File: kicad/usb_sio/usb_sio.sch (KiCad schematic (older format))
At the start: 24 parts, among them CON1 USB, P1 Z80_BUS_PINS, P2 IO_BUS_PINS, P3 CONN_02X05, U1 MCP2200, U2 68B50, U3 74HCT04, U4 1.8432MHz, Y1 12MHz

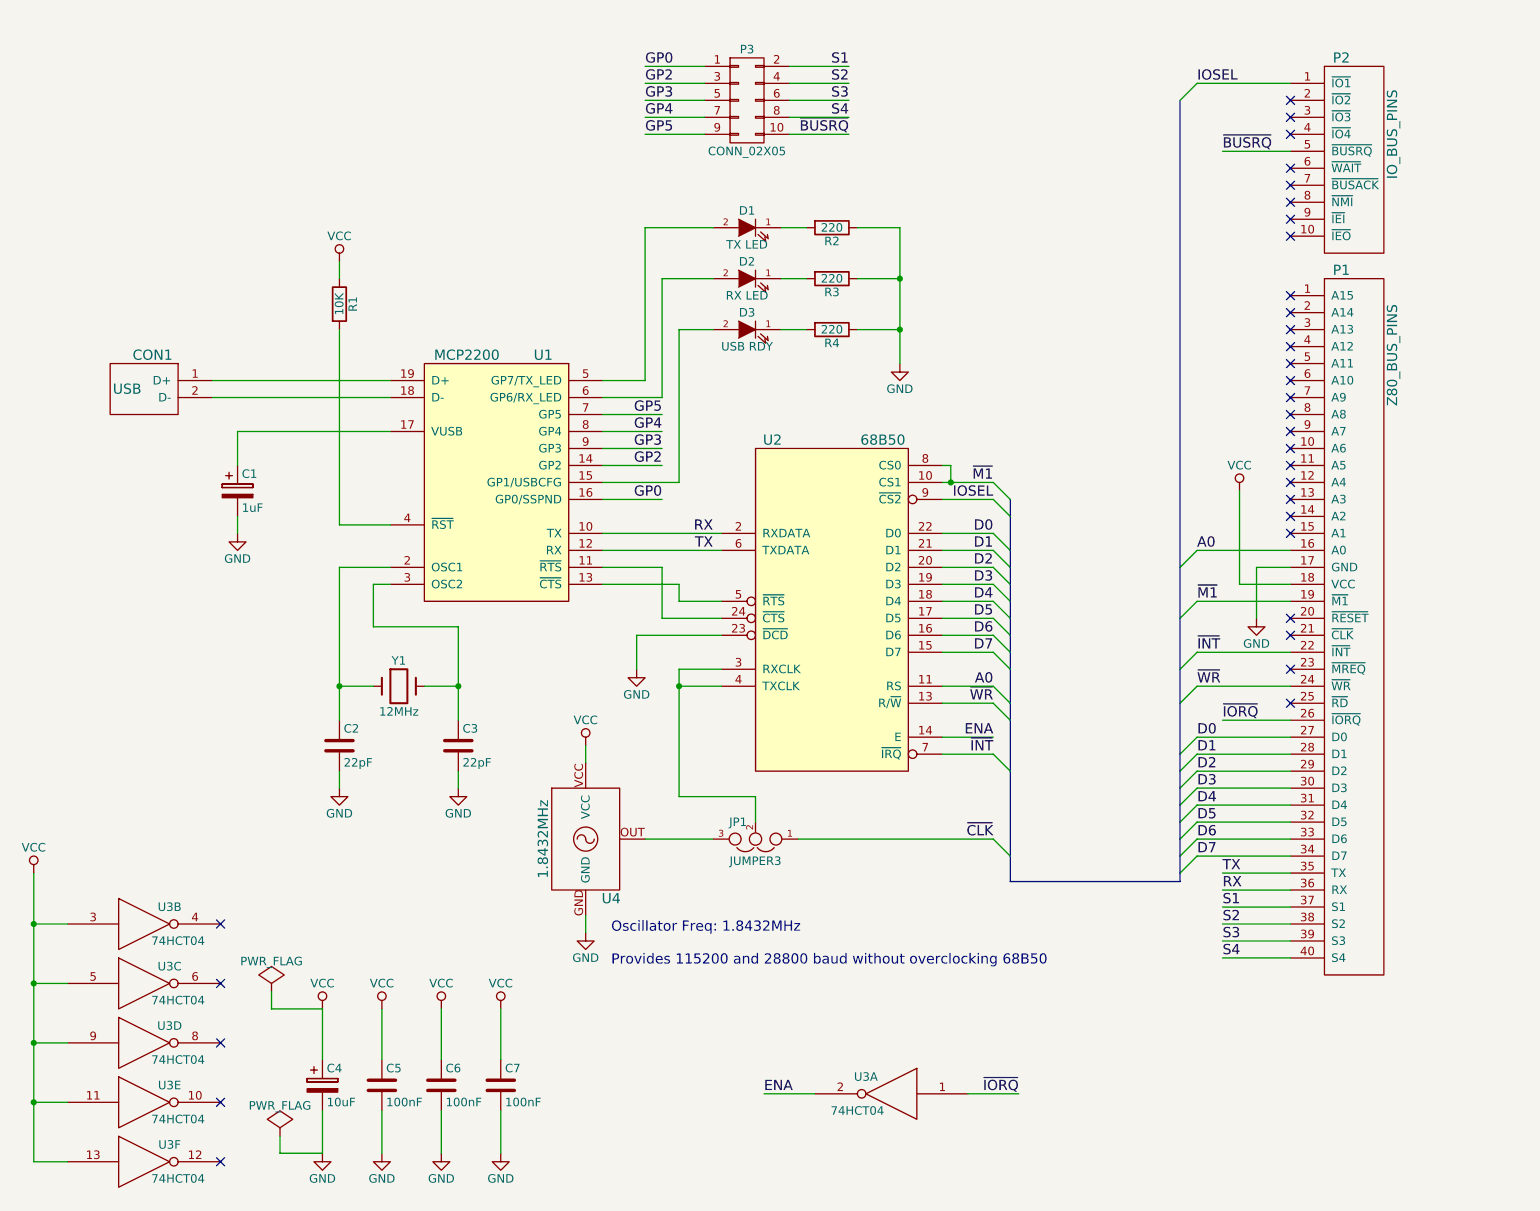
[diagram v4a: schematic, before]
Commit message: Fixed missing CLK like on SIO board
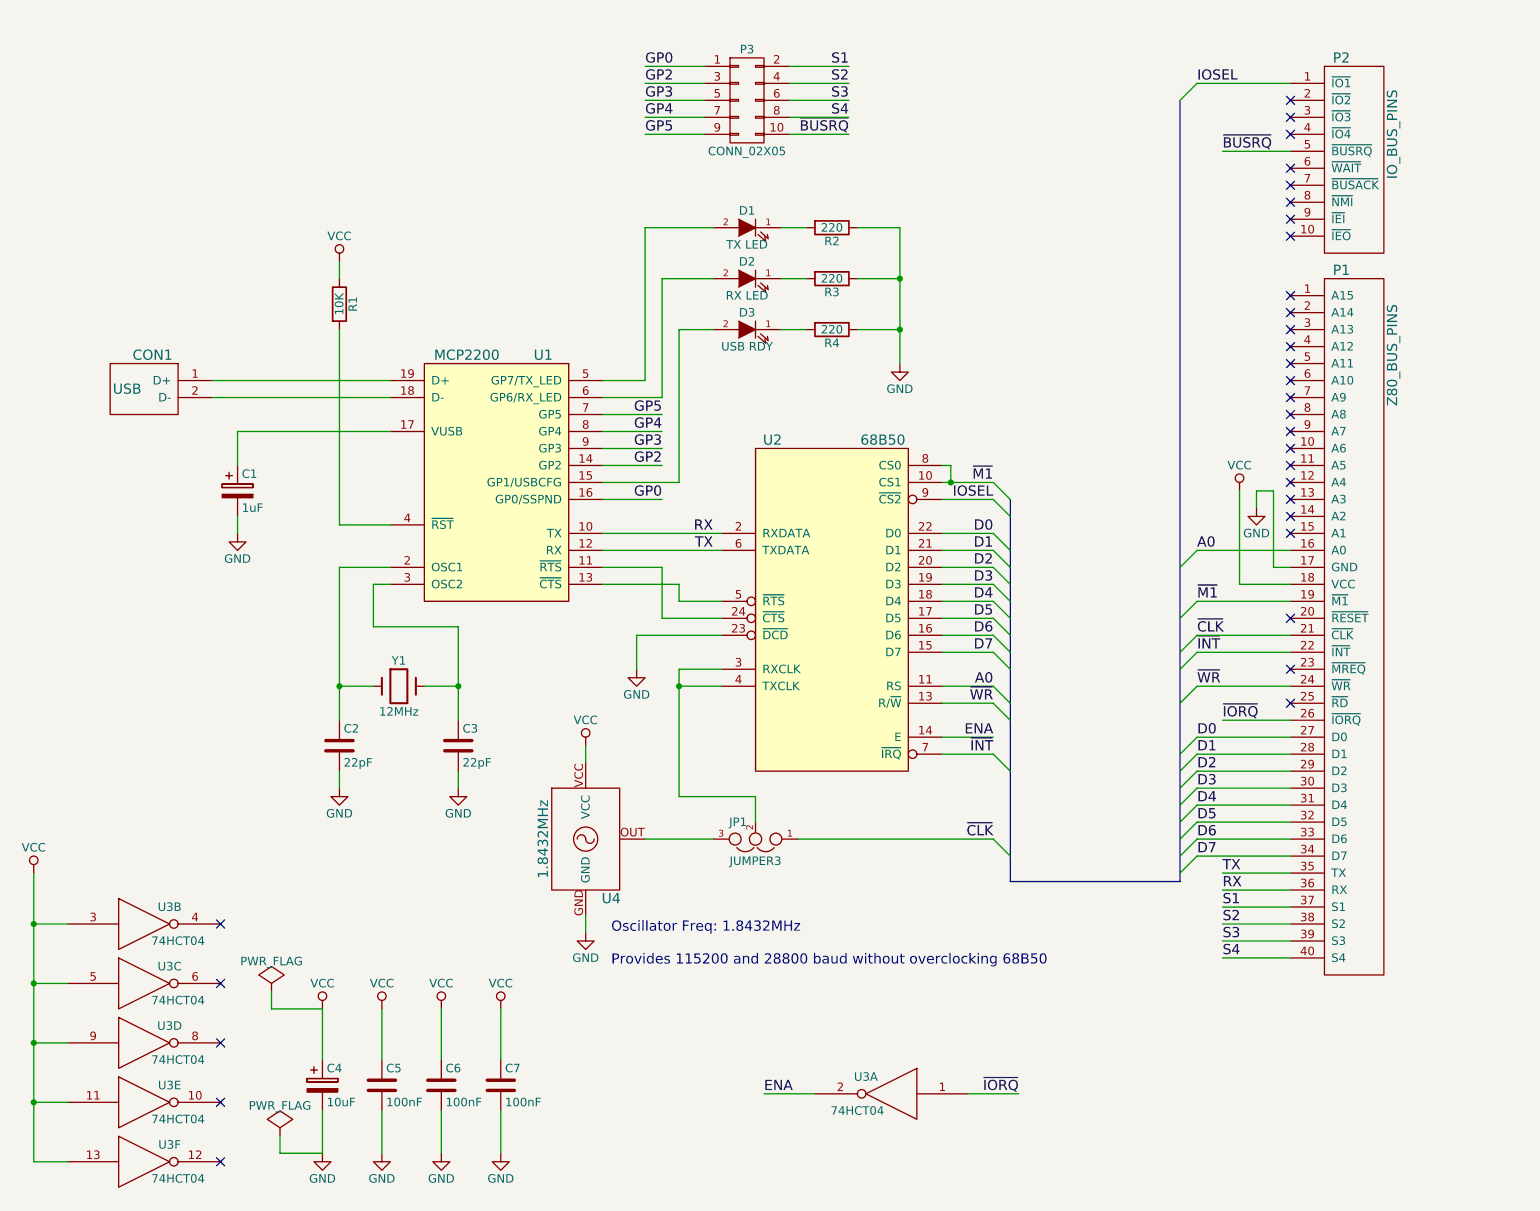
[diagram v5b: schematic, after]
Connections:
- net ~CLK: now also P1.21 (~CLK)
- no-connect marks 32 -> 31
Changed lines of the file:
@@
 NoConn ~ 8200 3700
 NoConn ~ 8200 4200
-NoConn ~ 8200 4300
 NoConn ~ 8200 4500
 NoConn ~ 8200 4700
@@
 L GND #PWR010
 U 1 1 57D54DB5
-P 8000 4200
-F 0 "#PWR010" H 8000 3950 50  0001 C CNN
-F 1 "GND" H 8000 4050 50  0000 C CNN
-F 2 "" H 8000 4200 50  0000 C CNN
-F 3 "" H 8000 4200 50  0000 C CNN
-	1    8000 4200
+P 8000 3550
+F 0 "#PWR010" H 8000 3300 50  0001 C CNN
+F 1 "GND" H 8000 3400 50  0000 C CNN
+F 2 "" H 8000 3550 50  0000 C CNN
+F 3 "" H 8000 3550 50  0000 C CNN
+	1    8000 3550
 	1    0    0    -1
 $EndComp
@@
 	2900 3900 2600 3900
 Wire Wire Line
-	2600 3900 2600 4600
-Wire Wire Line
-	2600 4600 2600 4800
+	2600 3900 2600 4800
 Wire Wire Line
 	2600 4600 2800 4600
@@
 	3100 4600 3300 4600
 Wire Wire Line
-	3300 4250 3300 4600
-Wire Wire Line
-	3300 4600 3300 4800
+	3300 4250 3300 4800
 Wire Wire Line
 	3300 4250 2800 4250
@@
 	4400 5500 4800 5500
 Wire Wire Line
-	4600 4500 4600 4600
-Wire Wire Line
-	4600 4600 4600 5250
+	4600 4500 4600 5250
 Wire Wire Line
 	4600 4500 4850 4500
@@
 	6150 4400 6450 4400
 Wire Bus Line
-	6550 3500 6550 3600
-Wire Bus Line
-	6550 3600 6550 3800
-Wire Bus Line
-	6550 3800 6550 3900
-Wire Bus Line
-	6550 3900 6550 4000
-Wire Bus Line
-	6550 4000 6550 4100
-Wire Bus Line
-	6550 4100 6550 4200
-Wire Bus Line
-	6550 4200 6550 4300
-Wire Bus Line
-	6550 4300 6550 4400
-Wire Bus Line
-	6550 4400 6550 4500
-Wire Bus Line
-	6550 4500 6550 4700
-Wire Bus Line
-	6550 4700 6550 4800
-Wire Bus Line
-	6550 4800 6550 5100
-Wire Bus Line
-	6550 5100 6550 5600
-Wire Bus Line
-	6550 5600 6550 5750
+	6550 3500 6550 5750
 Wire Bus Line
 	6550 5750 7550 5750
@@
 	6150 5000 6450 5000
 Wire Wire Line
-	6150 3400 6200 3400
-Wire Wire Line
-	6200 3400 6450 3400
+	6150 3400 6450 3400
 Wire Wire Line
 	6150 3500 6450 3500
@@
 	5300 5500 6450 5500
 Wire Bus Line
-	7550 5750 7550 5700
-Wire Bus Line
-	7550 5700 7550 5600
-Wire Bus Line
-	7550 5600 7550 5500
-Wire Bus Line
-	7550 5500 7550 5400
-Wire Bus Line
-	7550 5400 7550 5300
-Wire Bus Line
-	7550 5300 7550 5200
-Wire Bus Line
-	7550 5200 7550 5100
-Wire Bus Line
-	7550 5100 7550 5000
-Wire Bus Line
-	7550 5000 7550 4700
-Wire Bus Line
-	7550 4700 7550 4500
-Wire Bus Line
-	7550 4500 7550 4200
-Wire Bus Line
-	7550 4200 7550 3900
-Wire Bus Line
-	7550 3900 7550 1150
+	7550 5750 7550 1150
 Wire Wire Line
 	8200 1050 7650 1050
@@
 	5650 1900 5900 1900
 Wire Wire Line
-	5900 1900 5900 2200
-Wire Wire Line
-	5900 2200 5900 2500
-Wire Wire Line
-	5900 2500 5900 2700
+	5900 1900 5900 2700
 Wire Wire Line
 	5650 2500 5900 2500
@@
 	7800 1450 8200 1450
 Wire Wire Line
-	8200 3900 8000 3900
+	8100 3900 8200 3900
 Wire Wire Line
 	7900 4000 8200 4000
@@
 	7900 4000 7900 3450
 Wire Wire Line
-	8000 3900 8000 4200
-Wire Wire Line
 	6300 7000 6600 7000
 Wire Wire Line
 	8200 4800 7800 4800
 Wire Wire Line
-	800  5700 800  6000
-Wire Wire Line
-	800  6000 800  6350
-Wire Wire Line
-	800  6350 800  6700
-Wire Wire Line
-	800  6700 800  7050
-Wire Wire Line
-	800  7050 800  7400
+	800  5700 800  7400
 Wire Wire Line
 	800  7400 1000 7400
@@
 $EndComp
 Wire Wire Line
-	2500 6500 2500 6500
+	2200 6500 2500 6500
 Wire Wire Line
 	2500 6500 2500 6800
@@
 Wire Wire Line
 	2200 6400 2200 6500
-Wire Wire Line
-	2200 6500 2500 6500
-$Comp
-L PWR_FLAG #FLG?
+$Comp
+L PWR_FLAG #FLG021
 U 1 1 57D57677
 P 2250 7250
-F 0 "#FLG?" H 2250 7345 50  0001 C CNN
+F 0 "#FLG021" H 2250 7345 50  0001 C CNN
 F 1 "PWR_FLAG" H 2250 7430 50  0000 C CNN
 F 2 "" H 2250 7250 50  0000 C CNN
@@
 Wire Wire Line
 	2250 7350 2500 7350
+Wire Wire Line
+	8000 3550 8000 3450
+Wire Wire Line
+	8000 3450 8100 3450
+Wire Wire Line
+	8100 3450 8100 3900
+Entry Wire Line
+	7550 4400 7650 4300
+Wire Wire Line
+	7650 4300 8200 4300
+Text Label 7650 4300 0    60   ~ 0
+~CLK
 $EndSCHEMATC

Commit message: WIp on the SIO PCB
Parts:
- C1: footprint (none) -> Capacitors_ThroughHole:C_Radial_D5_L6_P2.5
- C2, C3: footprint (none) -> Capacitors_ThroughHole:C_Disc_D7.5_P5
- C4: footprint (none) -> Capacitors_ThroughHole:C_Radial_D6.3_L11.2_P2.5
- C5, C6, C7: footprint (none) -> Capacitors_ThroughHole:C_Disc_D3_P2.5
- CON1: footprint (none) -> Pin_Headers:Pin_Header_Angled_1x02
- D1, D2, D3: footprint (none) -> LEDs:LED-5MM
- JP1: footprint (none) -> Pin_Headers:Pin_Header_Straight_1x03
- P1: footprint (none) -> Pin_Headers:Pin_Header_Angled_1x40
- P2: footprint (none) -> Pin_Headers:Pin_Header_Angled_1x10
- P3: footprint (none) -> Pin_Headers:Pin_Header_Straight_2x05
- R1, R2, R3, R4: footprint (none) -> Resistors_ThroughHole:Resistor_Horizontal_RM10mm
- U1: footprint (none) -> Housings_DIP:DIP-20_W7.62mm_LongPads
- U2: footprint (none) -> Housings_DIP:DIP-24_W10.16mm_LongPads
- U3: footprint (none) -> Housings_DIP:DIP-14_W7.62mm_LongPads
- U4: footprint (none) -> Oscillators:OSC_DIP8
- Y1: footprint (none) -> Crystals:Crystal_HC49-U_Vertical
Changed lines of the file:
@@
 F 0 "U1" H 4100 2750 60  0000 C CNN
 F 1 "MCP2200" H 4550 2750 60  0000 C CNN
-F 2 "" H 3950 2900 60  0000 C CNN
+F 2 "Housings_DIP:DIP-20_W7.62mm_LongPads" H 3950 2900 60  0001 C CNN
 F 3 "" H 3950 2900 60  0000 C CNN
 	1    3950 2700
@@
 F 0 "C1" H 2025 3550 50  0000 L CNN
 F 1 "1uF" H 2025 3350 50  0000 L CNN
-F 2 "" H 2038 3300 50  0000 C CNN
+F 2 "Capacitors_ThroughHole:C_Radial_D5_L6_P2.5" H 2038 3300 50  0001 C CNN
 F 3 "" H 2000 3450 50  0000 C CNN
 	1    2000 3450
@@
 F 0 "Y1" H 2950 4750 50  0000 C CNN
 F 1 "12MHz" H 2950 4450 50  0000 C CNN
-F 2 "" H 2950 4600 50  0000 C CNN
+F 2 "Crystals:Crystal_HC49-U_Vertical" H 2950 4600 50  0001 C CNN
 F 3 "" H 2950 4600 50  0000 C CNN
 	1    2950 4600
@@
 F 0 "C2" H 2625 5050 50  0000 L CNN
 F 1 "22pF" H 2625 4850 50  0000 L CNN
-F 2 "" H 2638 4800 50  0000 C CNN
+F 2 "Capacitors_ThroughHole:C_Disc_D7.5_P5" H 2638 4800 50  0001 C CNN
 F 3 "" H 2600 4950 50  0000 C CNN
 	1    2600 4950
@@
 F 0 "C3" H 3325 5050 50  0000 L CNN
 F 1 "22pF" H 3325 4850 50  0000 L CNN
-F 2 "" H 3338 4800 50  0000 C CNN
+F 2 "Capacitors_ThroughHole:C_Disc_D7.5_P5" H 3338 4800 50  0001 C CNN
 F 3 "" H 3300 4950 50  0000 C CNN
 	1    3300 4950
@@
 F 0 "R1" V 2680 2350 50  0000 C CNN
 F 1 "10K" V 2600 2350 50  0000 C CNN
-F 2 "" V 2530 2350 50  0000 C CNN
+F 2 "Resistors_ThroughHole:Resistor_Horizontal_RM10mm" V 2530 2350 50  0001 C CNN
 F 3 "" H 2600 2350 50  0000 C CNN
 	1    2600 2350
@@
 F 0 "U2" H 5150 7050 60  0000 C CNN
 F 1 "68B50" H 5800 7050 60  0000 C CNN
-F 2 "" H 5350 5700 60  0000 C CNN
+F 2 "Housings_DIP:DIP-24_W10.16mm_LongPads" H 5350 5700 60  0001 C CNN
 F 3 "" H 5350 5700 60  0000 C CNN
 	1    5050 5100
@@
 F 0 "U4" H 4200 5750 60  0000 C CNN
 F 1 "1.8432MHz" V 3800 6100 60  0000 C CNN
-F 2 "" H 3850 5800 60  0000 C CNN
+F 2 "Oscillators:OSC_DIP8" H 3850 5800 60  0001 C CNN
 F 3 "" H 3850 5800 60  0000 C CNN
 	1    3850 5800
@@
 F 0 "JP1" H 5100 5400 50  0000 L CNN
 F 1 "JUMPER3" H 5050 5600 50  0000 C BNN
-F 2 "" H 5050 5500 50  0000 C CNN
+F 2 "Pin_Headers:Pin_Header_Straight_1x03" H 5050 5500 50  0001 C CNN
 F 3 "" H 5050 5500 50  0000 C CNN
 	1    5050 5500
@@
 F 0 "CON1" H 1800 2150 60  0000 C CNN
 F 1 "USB" H 1950 1950 60  0000 C CNN
-F 2 "" H 1650 2400 60  0000 C CNN
+F 2 "Pin_Headers:Pin_Header_Angled_1x02" H 1650 2400 60  0001 C CNN
 F 3 "" H 1650 2400 60  0000 C CNN
 	1    1650 2400
@@
 F 0 "P1" H 8500 2250 60  0000 C CNN
 F 1 "Z80_BUS_PINS" V 8800 1750 60  0000 C CNN
-F 2 "" H 8200 2300 60  0000 C CNN
+F 2 "Pin_Headers:Pin_Header_Angled_1x40" H 8200 2300 60  0001 C CNN
 F 3 "" H 8200 2300 60  0000 C CNN
 	1    8400 2200
@@
 F 0 "P2" H 8500 1000 60  0000 C CNN
 F 1 "IO_BUS_PINS" V 8800 550 60  0000 C CNN
-F 2 "" H 8400 1050 60  0000 C CNN
+F 2 "Pin_Headers:Pin_Header_Angled_1x10" H 8400 1050 60  0001 C CNN
 F 3 "" H 8400 1050 60  0000 C CNN
 	1    8400 950
@@
 F 0 "D2" H 5000 2300 50  0000 C CNN
 F 1 "RX LED" H 5000 2100 50  0000 C CNN
-F 2 "" H 5000 2200 50  0000 C CNN
+F 2 "LEDs:LED-5MM" H 5000 2200 50  0001 C CNN
 F 3 "" H 5000 2200 50  0000 C CNN
 	1    5000 2200
@@
 F 0 "D3" H 5000 2600 50  0000 C CNN
 F 1 "USB RDY" H 5000 2400 50  0000 C CNN
-F 2 "" H 5000 2500 50  0000 C CNN
+F 2 "LEDs:LED-5MM" H 5000 2500 50  0001 C CNN
 F 3 "" H 5000 2500 50  0000 C CNN
 	1    5000 2500
@@
 F 0 "D1" H 5000 2000 50  0000 C CNN
 F 1 "TX LED" H 5000 1800 50  0000 C CNN
-F 2 "" H 5000 1900 50  0000 C CNN
+F 2 "LEDs:LED-5MM" H 5000 1900 50  0001 C CNN
 F 3 "" H 5000 1900 50  0000 C CNN
 	1    5000 1900
@@
 F 0 "R2" V 5580 1900 50  0000 C CNN
 F 1 "220" V 5500 1900 50  0000 C CNN
-F 2 "" V 5430 1900 50  0000 C CNN
+F 2 "Resistors_ThroughHole:Resistor_Horizontal_RM10mm" V 5430 1900 50  0001 C CNN
 F 3 "" H 5500 1900 50  0000 C CNN
 	1    5500 1900
@@
 F 0 "R3" V 5580 2200 50  0000 C CNN
 F 1 "220" V 5500 2200 50  0000 C CNN
-F 2 "" V 5430 2200 50  0000 C CNN
+F 2 "Resistors_ThroughHole:Resistor_Horizontal_RM10mm" V 5430 2200 50  0001 C CNN
 F 3 "" H 5500 2200 50  0000 C CNN
 	1    5500 2200
@@
 F 0 "R4" V 5580 2500 50  0000 C CNN
 F 1 "220" V 5500 2500 50  0000 C CNN
-F 2 "" V 5430 2500 50  0000 C CNN
+F 2 "Resistors_ThroughHole:Resistor_Horizontal_RM10mm" V 5430 2500 50  0001 C CNN
 F 3 "" H 5500 2500 50  0000 C CNN
 	1    5500 2500
@@
 P 5000 1150
 F 0 "P3" H 5000 1450 50  0000 C CNN
-F 1 "CONN_02X05" H 5000 850 50  0000 C CNN
-F 2 "" H 5000 -50 50  0000 C CNN
+F 1 "CONN_02X05" H 5000 850 50  0001 C CNN
+F 2 "Pin_Headers:Pin_Header_Straight_2x05" H 5000 -50 50  0001 C CNN
 F 3 "" H 5000 -50 50  0000 C CNN
 	1    5000 1150
@@
 F 0 "U3" H 6000 7100 50  0000 C CNN
 F 1 "74HCT04" H 6050 6900 50  0000 C CNN
-F 2 "" H 5850 7000 50  0000 C CNN
+F 2 "Housings_DIP:DIP-14_W7.62mm_LongPads" H 5850 7000 50  0001 C CNN
 F 3 "" H 5850 7000 50  0000 C CNN
 	1    5850 7000
@@
 F 0 "U3" H 1600 6100 50  0000 C CNN
 F 1 "74HCT04" H 1650 5900 50  0000 C CNN
-F 2 "" H 1450 6000 50  0000 C CNN
+F 2 "Housings_DIP:DIP-14_W7.62mm_LongPads" H 1450 6000 50  0001 C CNN
 F 3 "" H 1450 6000 50  0000 C CNN
 	2    1450 6000
@@
 F 0 "U3" H 1600 6450 50  0000 C CNN
 F 1 "74HCT04" H 1650 6250 50  0000 C CNN
-F 2 "" H 1450 6350 50  0000 C CNN
+F 2 "Housings_DIP:DIP-14_W7.62mm_LongPads" H 1450 6350 50  0001 C CNN
 F 3 "" H 1450 6350 50  0000 C CNN
 	3    1450 6350
@@
 F 0 "U3" H 1600 6800 50  0000 C CNN
 F 1 "74HCT04" H 1650 6600 50  0000 C CNN
-F 2 "" H 1450 6700 50  0000 C CNN
+F 2 "Housings_DIP:DIP-14_W7.62mm_LongPads" H 1450 6700 50  0001 C CNN
 F 3 "" H 1450 6700 50  0000 C CNN
 	4    1450 6700
@@
 F 0 "U3" H 1600 7150 50  0000 C CNN
 F 1 "74HCT04" H 1650 6950 50  0000 C CNN
-F 2 "" H 1450 7050 50  0000 C CNN
+F 2 "Housings_DIP:DIP-14_W7.62mm_LongPads" H 1450 7050 50  0001 C CNN
 F 3 "" H 1450 7050 50  0000 C CNN
 	5    1450 7050
@@
 F 0 "U3" H 1600 7500 50  0000 C CNN
 F 1 "74HCT04" H 1650 7300 50  0000 C CNN
-F 2 "" H 1450 7400 50  0000 C CNN
+F 2 "Housings_DIP:DIP-14_W7.62mm_LongPads" H 1450 7400 50  0001 C CNN
 F 3 "" H 1450 7400 50  0000 C CNN
 	6    1450 7400
@@
 F 0 "C4" H 2525 7050 50  0000 L CNN
 F 1 "10uF" H 2525 6850 50  0000 L CNN
-F 2 "" H 2538 6800 50  0000 C CNN
+F 2 "Capacitors_ThroughHole:C_Radial_D6.3_L11.2_P2.5" H 2538 6800 50  0001 C CNN
 F 3 "" H 2500 6950 50  0000 C CNN
 	1    2500 6950
@@
 F 0 "C5" H 2875 7050 50  0000 L CNN
 F 1 "100nF" H 2875 6850 50  0000 L CNN
-F 2 "" H 2888 6800 50  0000 C CNN
+F 2 "Capacitors_ThroughHole:C_Disc_D3_P2.5" H 2888 6800 50  0001 C CNN
 F 3 "" H 2850 6950 50  0000 C CNN
 	1    2850 6950
@@
 F 0 "C6" H 3225 7050 50  0000 L CNN
 F 1 "100nF" H 3225 6850 50  0000 L CNN
-F 2 "" H 3238 6800 50  0000 C CNN
+F 2 "Capacitors_ThroughHole:C_Disc_D3_P2.5" H 3238 6800 50  0001 C CNN
 F 3 "" H 3200 6950 50  0000 C CNN
 	1    3200 6950
@@
 F 0 "C7" H 3575 7050 50  0000 L CNN
 F 1 "100nF" H 3575 6850 50  0000 L CNN
-F 2 "" H 3588 6800 50  0000 C CNN
+F 2 "Capacitors_ThroughHole:C_Disc_D3_P2.5" H 3588 6800 50  0001 C CNN
 F 3 "" H 3550 6950 50  0000 C CNN
 	1    3550 6950
